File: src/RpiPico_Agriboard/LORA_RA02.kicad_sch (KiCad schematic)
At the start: 2 parts, among them U6 Ai-Thinker-Ra-02

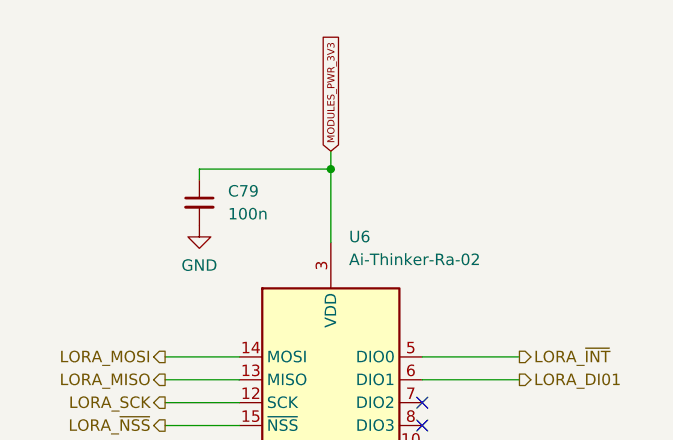
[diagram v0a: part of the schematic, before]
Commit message: Revert "schematic updates completed"
This reverts commit 0124993096667d53f20fd59dec80d3f5a1efcd43.
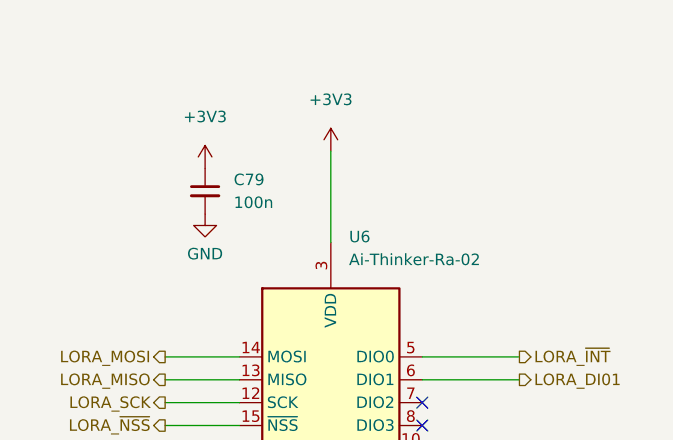
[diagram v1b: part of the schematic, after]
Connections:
- net MODULES_PWR_3V3 renamed +3V3
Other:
- moved on the sheet: C79
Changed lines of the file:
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@@
 (kicad_sch (version 20230121) (generator eeschema)
   (paper "A4")
-  (junction (at 151.765 53.4237) (diameter 0) (color 0 0 0 0)
-  )
   (no_connect (at 161.925 79.375))
   (no_connect (at 161.925 84.455))
   (no_connect (at 161.925 86.995))
   (no_connect (at 161.925 81.915))
-  (wire (pts (xy 137.16 54.61) (xy 137.16 53.4237))
-    (stroke (width 0) (type default))
-  )
-  (wire (pts (xy 151.765 53.4237) (xy 151.765 61.595))
-    (stroke (width 0) (type default))
-  )
   (wire (pts (xy 133.35 76.835) (xy 141.605 76.835))
     (stroke (width 0) (type default))
@@
     (stroke (width 0) (type default))
   )
-  (wire (pts (xy 151.765 51.435) (xy 151.765 53.4237))
-    (stroke (width 0) (type default))
-  )
-  (wire (pts (xy 137.16 53.4237) (xy 151.765 53.4237))
+  (wire (pts (xy 151.765 51.435) (xy 151.765 61.595))
     (stroke (width 0) (type default))
   )
   (wire (pts (xy 133.35 79.375) (xy 141.605 79.375))
     (stroke (width 0) (type default))
-  )
-  (global_label "MODULES_PWR_3V3" (shape input) (at 151.765 51.435 90) (fields_autoplaced)
-    (effects (font (size 0.8 0.8)) (justify left))
-    (property "Intersheetrefs" "${INTERSHEET_REFS}" (at 151.765 38.1381 90)
-      (effects (font (size 1.27 1.27)) (justify left) hide)
-    )
   )
   (hierarchical_label "LORA_DI01" (shape output) (at 172.72 76.835 0) (fields_autoplaced)
@@
     (effects (font (size 1.27 1.27)) (justify right))
   )
-  (symbol (lib_id "Device:C_Small") (at 137.16 57.15 0) (unit 1)
+  (symbol (lib_id "Device:C_Small") (at 137.795 55.88 0) (unit 1)
     (in_bom yes) (on_board yes) (dnp no) (fields_autoplaced)
-    (property "Reference" "C79" (at 140.335 55.8862 0)
+    (property "Reference" "C79" (at 140.97 54.6162 0)
       (effects (font (size 1.27 1.27)) (justify left))
     )
-    (property "Value" "100n" (at 140.335 58.4262 0)
+    (property "Value" "100n" (at 140.97 57.1562 0)
       (effects (font (size 1.27 1.27)) (justify left))
     )
-    (property "Footprint" "Capacitor_SMD:C_0402_1005Metric" (at 137.16 57.15 0)
+    (property "Footprint" "Capacitor_SMD:C_0402_1005Metric" (at 137.795 55.88 0)
       (effects (font (size 1.27 1.27)) hide)
     )
-    (property "Datasheet" "~" (at 137.16 57.15 0)
+    (property "Datasheet" "~" (at 137.795 55.88 0)
       (effects (font (size 1.27 1.27)) hide)
     )
@@
     )
   )
-  (symbol (lib_id "power:GND") (at 137.16 59.69 0) (unit 1)
+  (symbol (lib_id "power:GND") (at 137.795 58.42 0) (unit 1)
     (in_bom yes) (on_board yes) (dnp no) (fields_autoplaced)
-    (property "Reference" "#PWR0153" (at 137.16 66.04 0)
+    (property "Reference" "#PWR0153" (at 137.795 64.77 0)
       (effects (font (size 1.27 1.27)) hide)
     )
-    (property "Value" "GND" (at 137.16 64.135 0)
+    (property "Value" "GND" (at 137.795 62.865 0)
       (effects (font (size 1.27 1.27)))
     )
-    (property "Footprint" "" (at 137.16 59.69 0)
+    (property "Footprint" "" (at 137.795 58.42 0)
       (effects (font (size 1.27 1.27)) hide)
     )
-    (property "Datasheet" "" (at 137.16 59.69 0)
+    (property "Datasheet" "" (at 137.795 58.42 0)
       (effects (font (size 1.27 1.27)) hide)
     )
@@
         (path "/c2474b65-c0e8-4987-86b2-fddddd4113dc/4989adb0-6d03-42f9-a1c9-e7542d6be073"
           (reference "#PWR0153") (unit 1)
+        )
+      )
+    )
+  )
+  (symbol (lib_id "power:+3V3") (at 151.765 51.435 0) (unit 1)
+    (in_bom yes) (on_board yes) (dnp no) (fields_autoplaced)
+    (property "Reference" "#PWR0121" (at 151.765 55.245 0)
+      (effects (font (size 1.27 1.27)) hide)
+    )
+    (property "Value" "+3V3" (at 151.765 45.72 0)
+      (effects (font (size 1.27 1.27)))
+    )
+    (property "Footprint" "" (at 151.765 51.435 0)
+      (effects (font (size 1.27 1.27)) hide)
+    )
+    (property "Datasheet" "" (at 151.765 51.435 0)
+      (effects (font (size 1.27 1.27)) hide)
+    )
+    (pin "1")
+    (instances
+      (project "RpiPico_Agriboard"
+        (path "/c2474b65-c0e8-4987-86b2-fddddd4113dc/4989adb0-6d03-42f9-a1c9-e7542d6be073"
+          (reference "#PWR0121") (unit 1)
         )
       )
@@
         )
       )
+    )
+  )
+  (symbol (lib_id "power:+3V3") (at 137.795 53.34 0) (unit 1)
+    (in_bom yes) (on_board yes) (dnp no) (fields_autoplaced)
+    (property "Reference" "#PWR0152" (at 137.795 57.15 0)
+      (effects (font (size 1.27 1.27)) hide)
+    )
+    (property "Value" "+3V3" (at 137.795 47.625 0)
+      (effects (font (size 1.27 1.27)))
+    )
+    (property "Footprint" "" (at 137.795 53.34 0)
+      (effects (font (size 1.27 1.27)) hide)
+    )
+    (property "Datasheet" "" (at 137.795 53.34 0)
+      (effects (font (size 1.27 1.27)) hide)
+    )
+    (pin "1")
+    (instances
+      (project "RpiPico_Agriboard"
+        (path "/c2474b65-c0e8-4987-86b2-fddddd4113dc/4989adb0-6d03-42f9-a1c9-e7542d6be073"
+          (reference "#PWR0152") (unit 1)
+        )
+      )

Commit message: schematic updates completed
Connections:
- net +3V3 renamed MODULES_PWR_3V3
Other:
- moved on the sheet: C79
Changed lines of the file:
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@@
 (kicad_sch (version 20230121) (generator eeschema)
   (paper "A4")
+  (junction (at 151.765 53.4237) (diameter 0) (color 0 0 0 0)
+  )
   (no_connect (at 161.925 79.375))
   (no_connect (at 161.925 84.455))
   (no_connect (at 161.925 86.995))
   (no_connect (at 161.925 81.915))
+  (wire (pts (xy 137.16 54.61) (xy 137.16 53.4237))
+    (stroke (width 0) (type default))
+  )
+  (wire (pts (xy 151.765 53.4237) (xy 151.765 61.595))
+    (stroke (width 0) (type default))
+  )
   (wire (pts (xy 133.35 76.835) (xy 141.605 76.835))
     (stroke (width 0) (type default))
@@
     (stroke (width 0) (type default))
   )
-  (wire (pts (xy 151.765 51.435) (xy 151.765 61.595))
+  (wire (pts (xy 151.765 51.435) (xy 151.765 53.4237))
+    (stroke (width 0) (type default))
+  )
+  (wire (pts (xy 137.16 53.4237) (xy 151.765 53.4237))
     (stroke (width 0) (type default))
   )
   (wire (pts (xy 133.35 79.375) (xy 141.605 79.375))
     (stroke (width 0) (type default))
+  )
+  (global_label "MODULES_PWR_3V3" (shape input) (at 151.765 51.435 90) (fields_autoplaced)
+    (effects (font (size 0.8 0.8)) (justify left))
+    (property "Intersheetrefs" "${INTERSHEET_REFS}" (at 151.765 38.1381 90)
+      (effects (font (size 1.27 1.27)) (justify left) hide)
+    )
   )
   (hierarchical_label "LORA_DI01" (shape output) (at 172.72 76.835 0) (fields_autoplaced)
@@
     (effects (font (size 1.27 1.27)) (justify right))
   )
-  (symbol (lib_id "Device:C_Small") (at 137.795 55.88 0) (unit 1)
+  (symbol (lib_id "Device:C_Small") (at 137.16 57.15 0) (unit 1)
     (in_bom yes) (on_board yes) (dnp no) (fields_autoplaced)
-    (property "Reference" "C79" (at 140.97 54.6162 0)
+    (property "Reference" "C79" (at 140.335 55.8862 0)
       (effects (font (size 1.27 1.27)) (justify left))
     )
-    (property "Value" "100n" (at 140.97 57.1562 0)
+    (property "Value" "100n" (at 140.335 58.4262 0)
       (effects (font (size 1.27 1.27)) (justify left))
     )
-    (property "Footprint" "Capacitor_SMD:C_0402_1005Metric" (at 137.795 55.88 0)
+    (property "Footprint" "Capacitor_SMD:C_0402_1005Metric" (at 137.16 57.15 0)
       (effects (font (size 1.27 1.27)) hide)
     )
-    (property "Datasheet" "~" (at 137.795 55.88 0)
+    (property "Datasheet" "~" (at 137.16 57.15 0)
       (effects (font (size 1.27 1.27)) hide)
     )
@@
     )
   )
-  (symbol (lib_id "power:GND") (at 137.795 58.42 0) (unit 1)
+  (symbol (lib_id "power:GND") (at 137.16 59.69 0) (unit 1)
     (in_bom yes) (on_board yes) (dnp no) (fields_autoplaced)
-    (property "Reference" "#PWR0153" (at 137.795 64.77 0)
+    (property "Reference" "#PWR0153" (at 137.16 66.04 0)
       (effects (font (size 1.27 1.27)) hide)
     )
-    (property "Value" "GND" (at 137.795 62.865 0)
+    (property "Value" "GND" (at 137.16 64.135 0)
       (effects (font (size 1.27 1.27)))
     )
-    (property "Footprint" "" (at 137.795 58.42 0)
+    (property "Footprint" "" (at 137.16 59.69 0)
       (effects (font (size 1.27 1.27)) hide)
     )
-    (property "Datasheet" "" (at 137.795 58.42 0)
+    (property "Datasheet" "" (at 137.16 59.69 0)
       (effects (font (size 1.27 1.27)) hide)
     )
@@
         (path "/c2474b65-c0e8-4987-86b2-fddddd4113dc/4989adb0-6d03-42f9-a1c9-e7542d6be073"
           (reference "#PWR0153") (unit 1)
-        )
-      )
-    )
-  )
-  (symbol (lib_id "power:+3V3") (at 151.765 51.435 0) (unit 1)
-    (in_bom yes) (on_board yes) (dnp no) (fields_autoplaced)
-    (property "Reference" "#PWR0121" (at 151.765 55.245 0)
-      (effects (font (size 1.27 1.27)) hide)
-    )
-    (property "Value" "+3V3" (at 151.765 45.72 0)
-      (effects (font (size 1.27 1.27)))
-    )
-    (property "Footprint" "" (at 151.765 51.435 0)
-      (effects (font (size 1.27 1.27)) hide)
-    )
-    (property "Datasheet" "" (at 151.765 51.435 0)
-      (effects (font (size 1.27 1.27)) hide)
-    )
-    (pin "1")
-    (instances
-      (project "RpiPico_Agriboard"
-        (path "/c2474b65-c0e8-4987-86b2-fddddd4113dc/4989adb0-6d03-42f9-a1c9-e7542d6be073"
-          (reference "#PWR0121") (unit 1)
         )
       )
@@
         )
       )
-    )
-  )
-  (symbol (lib_id "power:+3V3") (at 137.795 53.34 0) (unit 1)
-    (in_bom yes) (on_board yes) (dnp no) (fields_autoplaced)
-    (property "Reference" "#PWR0152" (at 137.795 57.15 0)
-      (effects (font (size 1.27 1.27)) hide)
-    )
-    (property "Value" "+3V3" (at 137.795 47.625 0)
-      (effects (font (size 1.27 1.27)))
-    )
-    (property "Footprint" "" (at 137.795 53.34 0)
-      (effects (font (size 1.27 1.27)) hide)
-    )
-    (property "Datasheet" "" (at 137.795 53.34 0)
-      (effects (font (size 1.27 1.27)) hide)
-    )
-    (pin "1")
-    (instances
-      (project "RpiPico_Agriboard"
-        (path "/c2474b65-c0e8-4987-86b2-fddddd4113dc/4989adb0-6d03-42f9-a1c9-e7542d6be073"
-          (reference "#PWR0152") (unit 1)
-        )
-      )

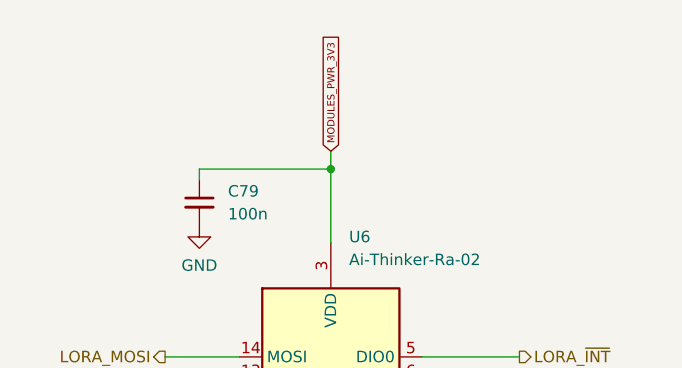
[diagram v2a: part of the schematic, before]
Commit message: power module supply line increase and reupdates on schematic
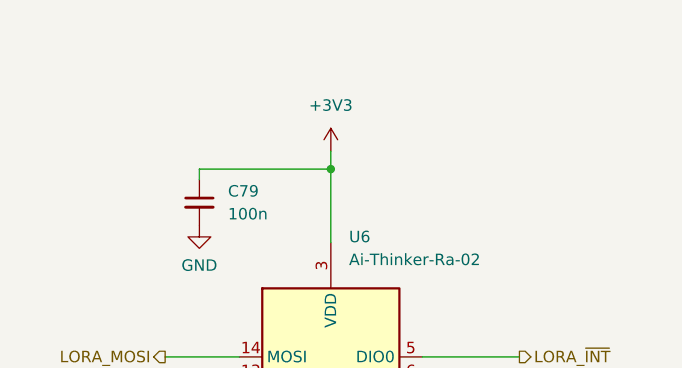
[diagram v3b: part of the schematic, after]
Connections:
- net MODULES_PWR_3V3 renamed +3V3
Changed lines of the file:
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@@
     (stroke (width 0) (type default))
-  )
-  (global_label "MODULES_PWR_3V3" (shape input) (at 151.765 51.435 90) (fields_autoplaced)
-    (effects (font (size 0.8 0.8)) (justify left))
-    (property "Intersheetrefs" "${INTERSHEET_REFS}" (at 151.765 38.1381 90)
-      (effects (font (size 1.27 1.27)) (justify left) hide)
-    )
   )
   (hierarchical_label "LORA_DI01" (shape output) (at 172.72 76.835 0) (fields_autoplaced)
@@
         )
       )
+    )
+  )
+  (symbol (lib_id "power:+3V3") (at 151.765 51.435 0) (mirror y) (unit 1)
+    (in_bom yes) (on_board yes) (dnp no) (fields_autoplaced)
+    (property "Reference" "#PWR0149" (at 151.765 55.245 0)
+      (effects (font (size 1.27 1.27)) hide)
+    )
+    (property "Value" "+3V3" (at 151.765 46.355 0)
+      (effects (font (size 1.27 1.27)))
+    )
+    (property "Footprint" "" (at 151.765 51.435 0)
+      (effects (font (size 1.27 1.27)) hide)
+    )
+    (property "Datasheet" "" (at 151.765 51.435 0)
+      (effects (font (size 1.27 1.27)) hide)
+    )
+    (pin "1")
+    (instances
+      (project "RpiPico_Agriboard"
+        (path "/c2474b65-c0e8-4987-86b2-fddddd4113dc/ca6d2227-669d-49ee-b832-d83811a1c959"
+          (reference "#PWR0149") (unit 1)
+        )
+        (path "/c2474b65-c0e8-4987-86b2-fddddd4113dc/4989adb0-6d03-42f9-a1c9-e7542d6be073"
+          (reference "#PWR017") (unit 1)
+        )
+      )

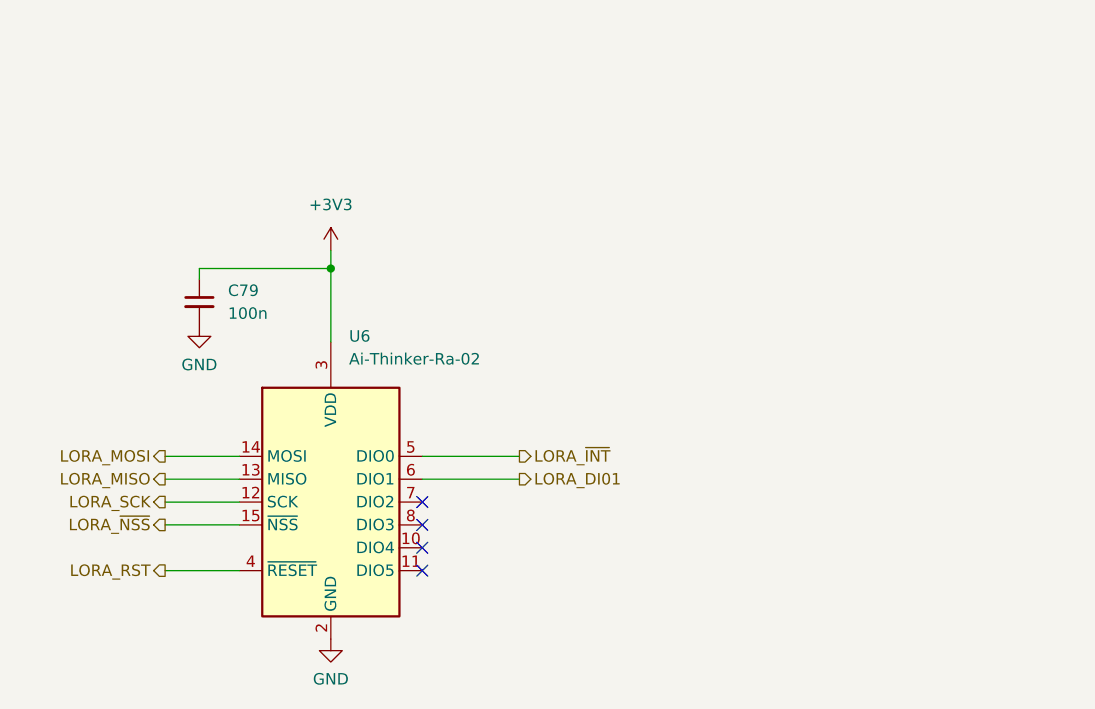
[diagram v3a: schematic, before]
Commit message: complete board update and routing
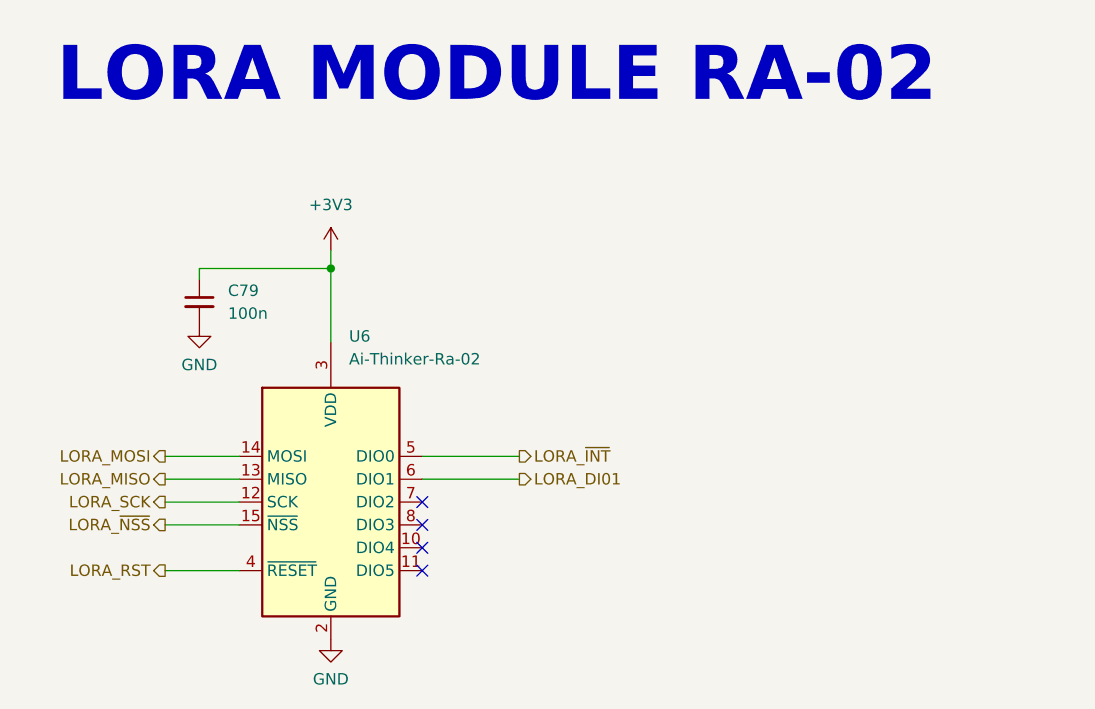
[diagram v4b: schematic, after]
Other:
- note added: "LORA MODULE RA-02"
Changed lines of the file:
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@@
     (stroke (width 0) (type default))
+  )
+  (text "LORA MODULE RA-02" (at 121.285 35.56 0)
+    (effects (font (face "Agency FB") (size 6 6) bold) (justify left bottom))
   )
   (hierarchical_label "LORA_DI01" (shape output) (at 172.72 76.835 0) (fields_autoplaced)
